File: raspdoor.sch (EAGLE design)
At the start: 26 parts, among them IC1 ATMEGA168-PU, IC2 ENC28J60SP, J1 1X2-3.5MM

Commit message: Added ENC28J60 connections to board
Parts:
- added C10, C11: 10pF, adafruit:C-USC0805
- added C12: 10uF, adafruit:C-USC0805
- added Q1: (no value), adafruit:CRYSTALHC49S
- added R7: 2.32k, adafruit:R-US_R0805
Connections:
- new net CS: IC1.DIGITAL_8, IC2.!CS
- new net N$10: C10.1, IC2.OSC1, Q1.1
- new net N$11: C11.1, IC2.OSC2, Q1.2
- new net N$12: C12.1, IC2.VCAP
- new net N$9: IC2.RBIAS, R7.2
- new net NETRESET: IC1.DIGITAL_7, IC2.!RESET
- new net SCK: IC1.DIGITAL_13, IC2.SCK
- new net SI: IC1.DIGITAL_11(PWM), IC2.SI
- new net SO: IC1.DIGITAL_12, IC2.SO
- net +3V3: now also IC2.VDD, IC2.VDDOSC, IC2.VDDPLL, IC2.VDDRX, IC2.VDDTX
- net GND: now also C10.2, C11.2, C12.2, IC2.VSS, IC2.VSSOSC, IC2.VSSPLL, IC2.VSSRX, IC2.VSSTX, R7.1
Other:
- moved on the sheet: C5, C6, C7, C8, C9, CLOCK, FTDI, IC1, IC2, R1, R2, R3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

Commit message: Minor changes
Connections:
- new net MOSFET: IC1.DIGITAL_3(PWM)
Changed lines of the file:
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@@
+</segment>
+</net>
+<net name="MOSFET" class="0">
+<segment>
+<pinref part="IC1" gate="1" pin="DIGITAL_3(PWM)"/>
+<wire x1="78.74" y1="83.82" x2="93.98" y2="83.82" width="0.1524" layer="91"/>
+<label x="81.28" y="83.82" size="1.778" layer="95"/>
 </segment>
 </net>

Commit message: Initial Board + RFID Terminals
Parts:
- added D2: (no value), adafruit:DIODESMA
- added J2, J3, J4, J5: 1X2-3.5MM, adafruit:1X2-3.5MM
- added OPEN, PWR: (no value), adafruit:LEDCHIPLED_0805
- added Q2: MOSFET-NCHANNELFQP30N06L, SparkFun-DiscreteSemi:MOSFET-NCHANNELFQP30N06L
- added R10, R9: 150, adafruit:R-US_R0805
- added R8: 10k, adafruit:R-US_R0805
- added S1, S3: STANDOFF_ELECTRICAL, SparkFun-Electromechanical:STANDOFF_ELECTRICAL
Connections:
- new net BUZZER: IC1.DIGITAL_4, J4.2
- new net D0: IC1.DIGITAL_2, J3.2
- new net D1: IC1.DIGITAL_3(PWM), J4.1
- new net LED: IC1.DIGITAL_5(PWM), J5.1
- new net N$14: D2.A, J2.2, Q2.D
- new net N$15: PWR.A, R9.1
- new net N$16: OPEN.A, R10.2
- net +5V: now also J3.1, R9.2
- net GND: now also J5.2, OPEN.C, PWR.C, Q2.S, R8.1
- net MOSFET: now also IC1.DIGITAL_6(PWM), Q2.G, R10.1, R8.2; no longer IC1.DIGITAL_3(PWM)
- net VCC: now also D2.C, J2.1
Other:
- note added: "5V"
- note added: "Buzzer"
- note added: "D0"
- note added: "D1"
- note added: "GND"
- note added: "LED"
- moved on the sheet: 5VREG, B1, C1, C2, C3

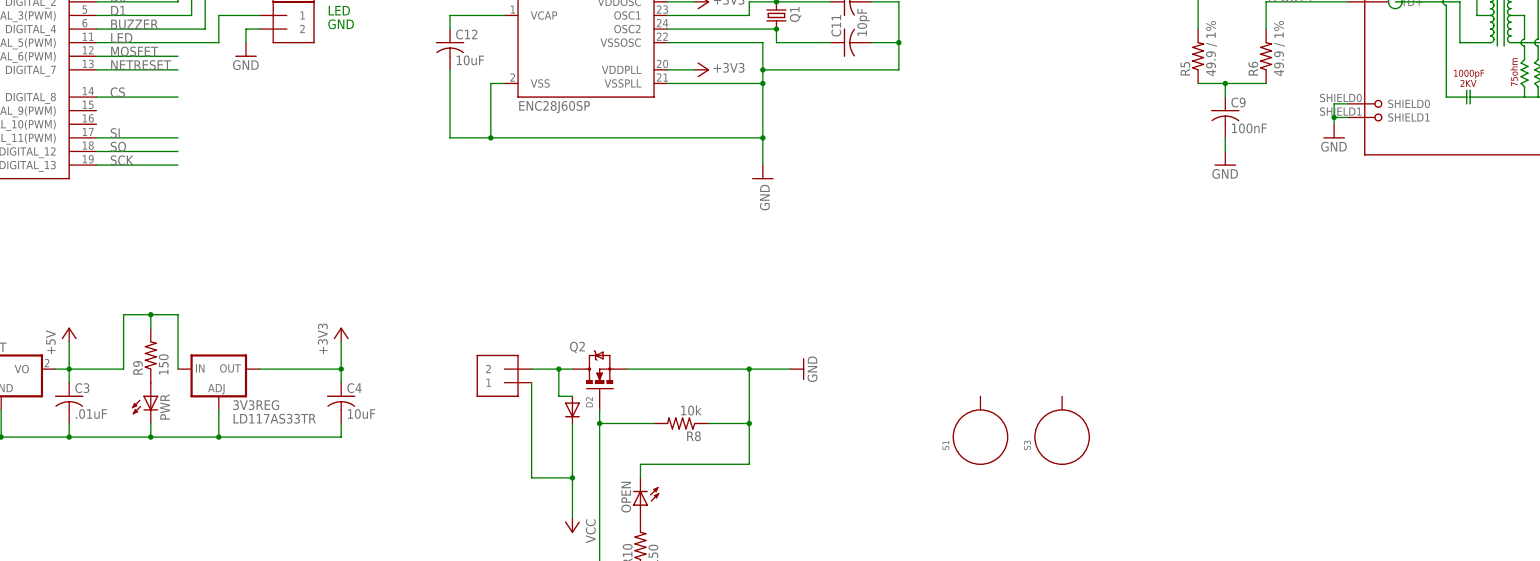
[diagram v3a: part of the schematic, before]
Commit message: Added an override button to schematic and PCB.
Allows for the hookup of a switch that will override RFID and cause
action in code immediately.
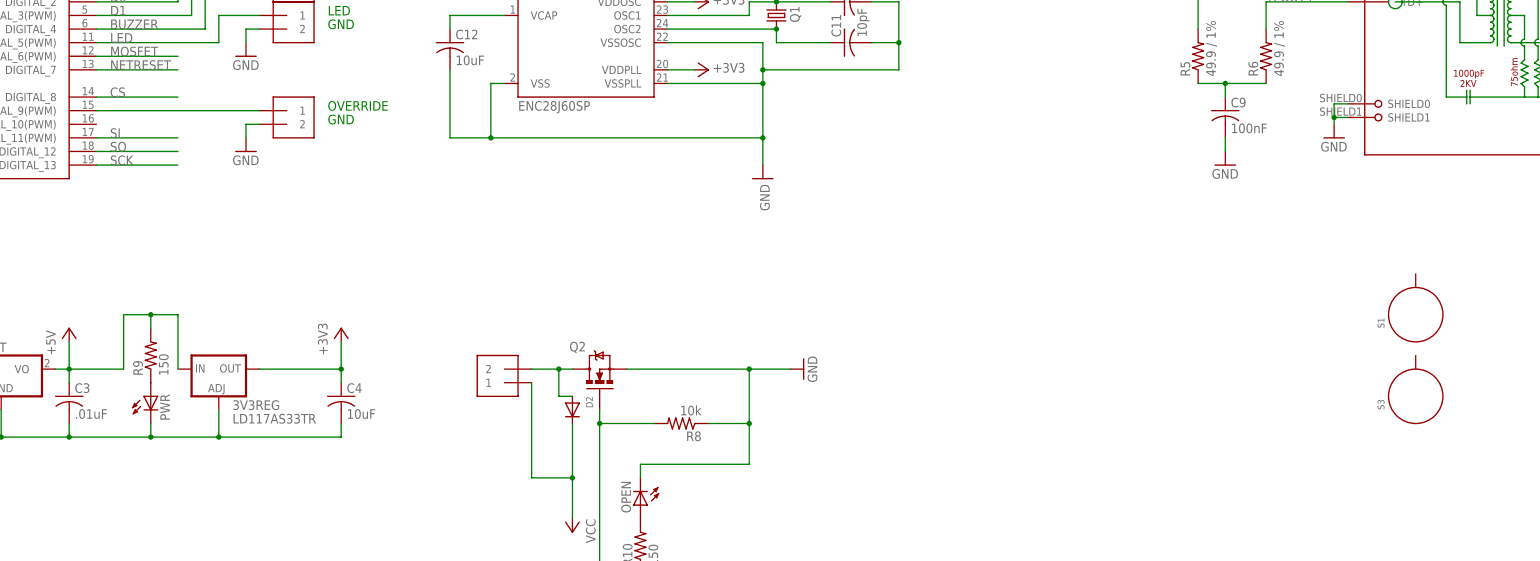
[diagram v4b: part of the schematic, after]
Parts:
- added J6: 1X2-3.5MM, adafruit:1X2-3.5MM
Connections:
- new net N$17: IC1.DIGITAL_9(PWM), J6.1
- net GND: now also J6.2
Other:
- note added: "OVERRIDE"
- moved on the sheet: S1, S3
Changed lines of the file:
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@@
 <part name="GND15" library="supply1" deviceset="GND" device=""/>
 <part name="P+7" library="supply1" deviceset="+5V" device=""/>
+<part name="J6" library="adafruit" deviceset="1X2" device="-3.5MM"/>
+<part name="GND16" library="supply1" deviceset="GND" device=""/>
 </parts>
 <sheets>
@@
 <text x="121.92" y="83.82" size="1.778" layer="91">LED</text>
 <text x="121.92" y="81.28" size="1.778" layer="91">GND</text>
+<text x="121.92" y="66.04" size="1.778" layer="91">OVERRIDE</text>
+<text x="121.92" y="63.5" size="1.778" layer="91">GND</text>
 </plain>
 <instances>
@@
 <instance part="R8" gate="G$1" x="187.96" y="7.62" rot="R180"/>
 <instance part="D2" gate="G$1" x="167.64" y="10.16" rot="R270"/>
-<instance part="S1" gate="G$1" x="243.84" y="5.08" rot="R90"/>
-<instance part="S3" gate="G$1" x="259.08" y="5.08" rot="R90"/>
+<instance part="S1" gate="G$1" x="325.12" y="27.94" rot="R90"/>
+<instance part="S3" gate="G$1" x="325.12" y="12.7" rot="R90"/>
 <instance part="PWR" gate="G$1" x="88.9" y="12.7"/>
 <instance part="OPEN" gate="G$1" x="180.34" y="-7.62" rot="R180"/>
@@
 <attribute name="VALUE" x="109.22" y="106.68" size="1.778" layer="96" rot="R180"/>
 </instance>
+<instance part="J6" gate="G$1" x="114.3" y="63.5"/>
+<instance part="GND16" gate="1" x="106.68" y="58.42"/>
 </instances>
 <busses>
@@
 <segment>
 <pinref part="GND15" gate="1" pin="GND"/>
+<pinref part="J5" gate="G$1" pin="2"/>
 <wire x1="106.68" y1="78.74" x2="106.68" y2="81.28" width="0.1524" layer="91"/>
-<pinref part="J5" gate="G$1" pin="2"/>
 <wire x1="106.68" y1="81.28" x2="109.22" y2="81.28" width="0.1524" layer="91"/>
+</segment>
+<segment>
+<pinref part="GND16" gate="1" pin="GND"/>
+<wire x1="106.68" y1="60.96" x2="106.68" y2="63.5" width="0.1524" layer="91"/>
+<pinref part="J6" gate="G$1" pin="2"/>
+<wire x1="106.68" y1="63.5" x2="109.22" y2="63.5" width="0.1524" layer="91"/>
 </segment>
 </net>
@@
 </segment>
 </net>
+<net name="N$17" class="0">
+<segment>
+<pinref part="IC1" gate="1" pin="DIGITAL_9(PWM)"/>
+<pinref part="J6" gate="G$1" pin="1"/>
+<wire x1="78.74" y1="66.04" x2="109.22" y2="66.04" width="0.1524" layer="91"/>
+</segment>
+</net>
